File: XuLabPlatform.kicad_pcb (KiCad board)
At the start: 2 copper layers, 0 parts

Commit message: Add initial PCB layout
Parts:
- added C1: 4.7uF, Capacitor_SMD:C_0603_1608Metric, F.Cu at (143.0, 53.2)
- added C10: 100nF, Capacitor_SMD:C_0402_1005Metric, F.Cu at (122.5, 61.5)
- added C11: 22pF, Capacitor_SMD:C_0402_1005Metric, F.Cu at (141.2, 55.2)
- added C12: 22pF, Capacitor_SMD:C_0402_1005Metric, F.Cu at (137.2, 57.8)
- added C13: 100nF, Capacitor_SMD:C_0402_1005Metric, F.Cu at (167.5, 76.4)
- added C14: 100nF, Capacitor_SMD:C_0402_1005Metric, F.Cu at (165.0, 77.2)
- added C15: 1uF, Capacitor_SMD:C_0603_1608Metric, F.Cu at (129.0, 68.0)
- added C16: 10uF, Capacitor_SMD:C_1206_3216Metric, F.Cu at (130.0, 75.0)
- added C17: 100nF, Capacitor_SMD:C_0402_1005Metric, F.Cu at (129.0, 53.0)
- added C18: 100uF, Capacitor_SMD:C_1210_3225Metric, F.Cu at (161.5, 125.0)
- added C19: 10uF, Capacitor_SMD:C_1206_3216Metric, F.Cu at (165.0, 125.0)
- added C2: 100nF, Capacitor_SMD:C_0402_1005Metric, F.Cu at (144.0, 56.5)
- added C20: 1uF, Capacitor_SMD:C_0603_1608Metric, F.Cu at (163.0, 128.5)
- added C21: 10uF, Capacitor_SMD:C_1206_3216Metric, F.Cu at (150.0, 85.0)
- added C22: 100nF, Capacitor_SMD:C_0402_1005Metric, F.Cu at (152.5, 79.5)
- added C23: 22uF, Capacitor_SMD:C_0603_1608Metric, F.Cu at (154.5, 85.0)
- added C24: 22uF, Capacitor_SMD:C_0603_1608Metric, F.Cu at (154.5, 87.0)
- added C25: 100nF, Capacitor_SMD:C_0402_1005Metric, F.Cu at (158.0, 62.0)
- added C3: 100nF, Capacitor_SMD:C_0402_1005Metric, F.Cu at (146.2, 54.0)
- added C4: 100nF, Capacitor_SMD:C_0402_1005Metric, F.Cu at (156.5, 57.0)
- added C5: 100nF, Capacitor_SMD:C_0402_1005Metric, F.Cu at (155.0, 68.5)
- added C6: 100nF, Capacitor_SMD:C_0402_1005Metric, F.Cu at (147.0, 69.5)
- added C7: 2.2uF, Capacitor_SMD:C_0603_1608Metric, F.Cu at (152.8, 70.5)
- added C8: 1uF, Capacitor_SMD:C_0603_1608Metric, F.Cu at (138.5, 63.2)
- added C9: 100nF, Capacitor_SMD:C_0402_1005Metric, F.Cu at (142.5, 63.8)
- added CR1: SMBJ7.5A-13-F, XuLab:SMB_DIO, F.Cu at (150.0, 117.0)
- added CR2: MSP3V3-M3/89A, XuLab:DO-219AD_VIS, F.Cu at (161.0, 84.0)
- added D1: LED, LED_SMD:LED_0603_1608Metric, F.Cu at (158.5, 68.5)
- added D2: 75 A, Package_TO_SOT_THT:TO-247-2_Vertical, F.Cu at (155.4, 125.2)
- added D3: RCLAMP0582B, Package_TO_SOT_SMD:SOT-416, F.Cu at (163.0, 54.5)
- added FB1: 200 @ 100 MHz, Inductor_SMD:L_0805_2012Metric, F.Cu at (140.5, 63.0)
- added FL1: 0805USB-502MLC, Inductor_SMD:L_CommonModeChoke_Coilcraft_0805USB, F.Cu at (167.5, 58.5)
- added J1: SWD Connector, Connector_IDC:IDC-Header_2x05_P2.54mm_Vertical, F.Cu at (183.4, 53.6)
- added J10: Servo7, TerminalBlock_Phoenix:TerminalBlock_Phoenix_MKDS-1,5-3-5.08_1x03_P5.08mm_Horizontal, F.Cu at (185.0, 115.0)
- added J11: Servo8, TerminalBlock_Phoenix:TerminalBlock_Phoenix_MKDS-1,5-3-5.08_1x03_P5.08mm_Horizontal, F.Cu at (185.0, 98.6)
- added J12: Thruster SGN, Connector_JST:JST_VH_B3P-VH_1x03_P3.96mm_Vertical, F.Cu at (185.5, 72.5)
- added J13: USB_B_Micro, Connector_USB:USB_Micro-B_Molex_47346-0001, F.Cu at (167.4, 49.8)
- added J2: Conn_01x04, Connector_JST:JST_GH_BM04B-GHS-TBT_1x04-1MP_P1.25mm_Vertical, F.Cu at (133.0, 50.0)
- added J3: 1986660-2, XuLab:CONN2_1986660-2_TEC, F.Cu at (145.1, 133.8)
- added J4: Servo1, TerminalBlock_Phoenix:TerminalBlock_Phoenix_MKDS-1,5-3-5.08_1x03_P5.08mm_Horizontal, F.Cu at (115.0, 137.5)
- added J5: Servo2, TerminalBlock_Phoenix:TerminalBlock_Phoenix_MKDS-1,5-3-5.08_1x03_P5.08mm_Horizontal, F.Cu at (115.0, 121.0)
- added J6: Servo3, TerminalBlock_Phoenix:TerminalBlock_Phoenix_MKDS-1,5-3-5.08_1x03_P5.08mm_Horizontal, F.Cu at (115.0, 104.6)
- added J7: Servo4, TerminalBlock_Phoenix:TerminalBlock_Phoenix_MKDS-1,5-3-5.08_1x03_P5.08mm_Horizontal, F.Cu at (115.0, 88.2)
- added J8: Servo5, TerminalBlock_Phoenix:TerminalBlock_Phoenix_MKDS-1,5-3-5.08_1x03_P5.08mm_Horizontal, F.Cu at (185.0, 147.8)
- added J9: Servo6, TerminalBlock_Phoenix:TerminalBlock_Phoenix_MKDS-1,5-3-5.08_1x03_P5.08mm_Horizontal, F.Cu at (185.0, 131.4)
- added L1: 3.9uH, Inductor_SMD:L_Pulse_PA4334, F.Cu at (154.5, 82.0)
- added R1: 10k, Resistor_SMD:R_0402_1005Metric, F.Cu at (115.5, 75.0)
- added R2: 10k, Resistor_SMD:R_0402_1005Metric, F.Cu at (115.5, 82.0)
- added R3: 270, Resistor_SMD:R_0402_1005Metric, F.Cu at (141.2, 60.2)
- added R4: 4k7, Resistor_SMD:R_0402_1005Metric, F.Cu at (150.0, 52.0)
- added R5: 4k7, Resistor_SMD:R_0402_1005Metric, F.Cu at (148.0, 52.0)
- added R6: 22, Resistor_SMD:R_0402_1005Metric, F.Cu at (158.0, 59.0)
- added R7: 22, Resistor_SMD:R_0402_1005Metric, F.Cu at (158.0, 60.5)
- added R8: 75, Resistor_SMD:R_0402_1005Metric, F.Cu at (158.5, 71.5)
- added SW1: SW_Push, Button_Switch_SMD:SW_Push_1P1T_NO_E-Switch_TL3301NxxxxxG, F.Cu at (115.5, 61.5)
- added SW2: SW_SPDT, Button_Switch_SMD:Nidec_Copal_CAS-120A, F.Cu at (115.5, 71.5)
- added SW3: SW_SPDT, Button_Switch_SMD:Nidec_Copal_CAS-120A, F.Cu at (115.5, 78.5)
- added TP1: TestPoint, TestPoint:TestPoint_Plated_Hole_D2.0mm, F.Cu at (130.0, 120.0)
- added TP2: TestPoint, TestPoint:TestPoint_Plated_Hole_D2.0mm, F.Cu at (140.5, 82.5)
- added TP3: TestPoint, TestPoint:TestPoint_Plated_Hole_D2.0mm, F.Cu at (135.0, 120.0)
- added TP4: TestPoint, TestPoint:TestPoint_Plated_Hole_D2.0mm, F.Cu at (165.0, 67.5)
- added TP5: TestPoint, TestPoint:TestPoint_Plated_Hole_D2.0mm, F.Cu at (135.5, 82.5)
- added U1: STM32F446RCTx, Package_QFP:LQFP-64_10x10mm_P0.5mm, F.Cu at (150.0, 62.0)
- added U2: ISM330DHCX, Package_LGA:LGA-14_3x2.5mm_P0.5mm_LayoutBorder3x4y, F.Cu at (165.0, 75.0)
- added U3: MMC5983MA, XuLab:MMC5983MA_MEM, F.Cu at (130.0, 71.0)
- added U4: AP63203WU, Package_TO_SOT_SMD:TSOT-23-6, F.Cu at (150.0, 82.0)
- added U5: TVS0500DRV, Package_SON:WSON-6-1EP_2x2mm_P0.65mm_EP1x1.6mm, F.Cu at (171.0, 54.0)
- added Y1: 25 MHz, Crystal:Crystal_SMD_Abracon_ABM8G-4Pin_3.2x2.5mm, F.Cu at (140.2, 57.8)
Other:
- board outline added: 83 x 105 mm

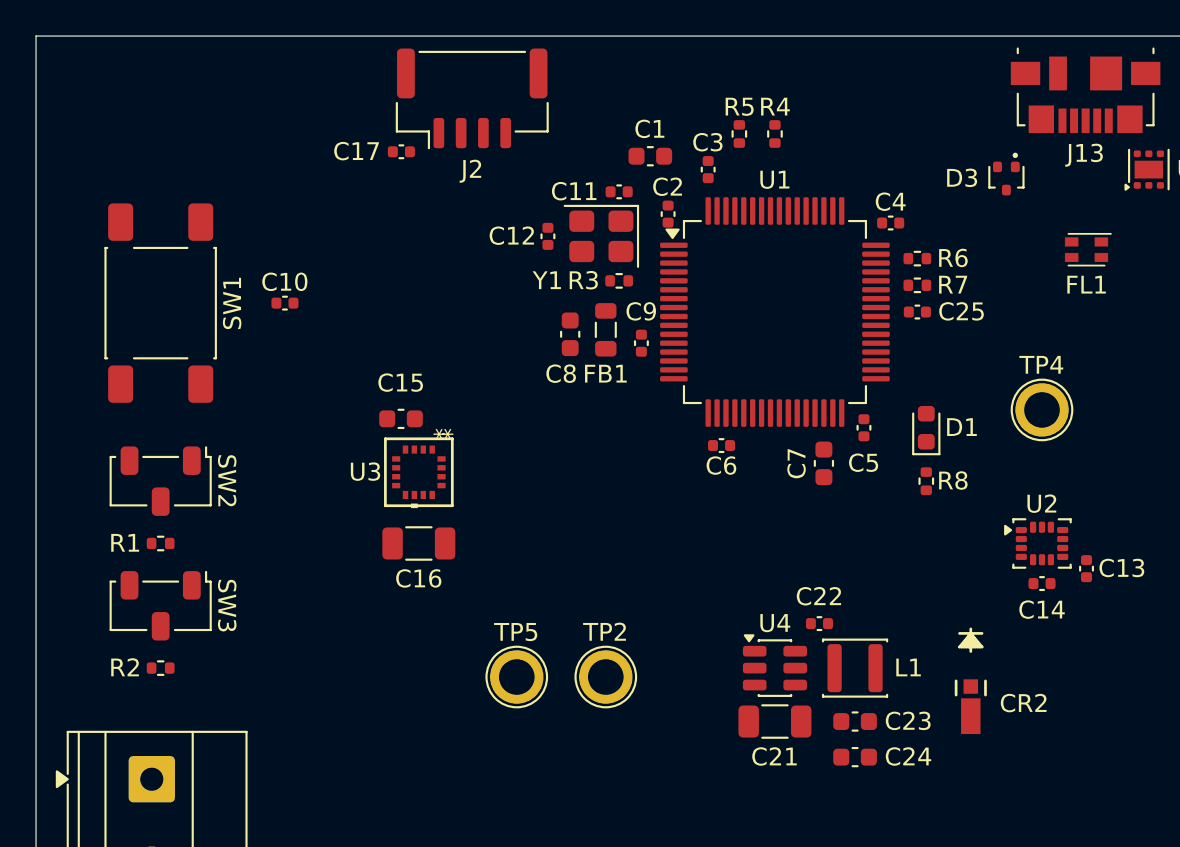
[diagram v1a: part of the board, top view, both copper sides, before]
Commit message: Change ferrite bead with TLV1117LV33 LDO for 3.3VA filtering
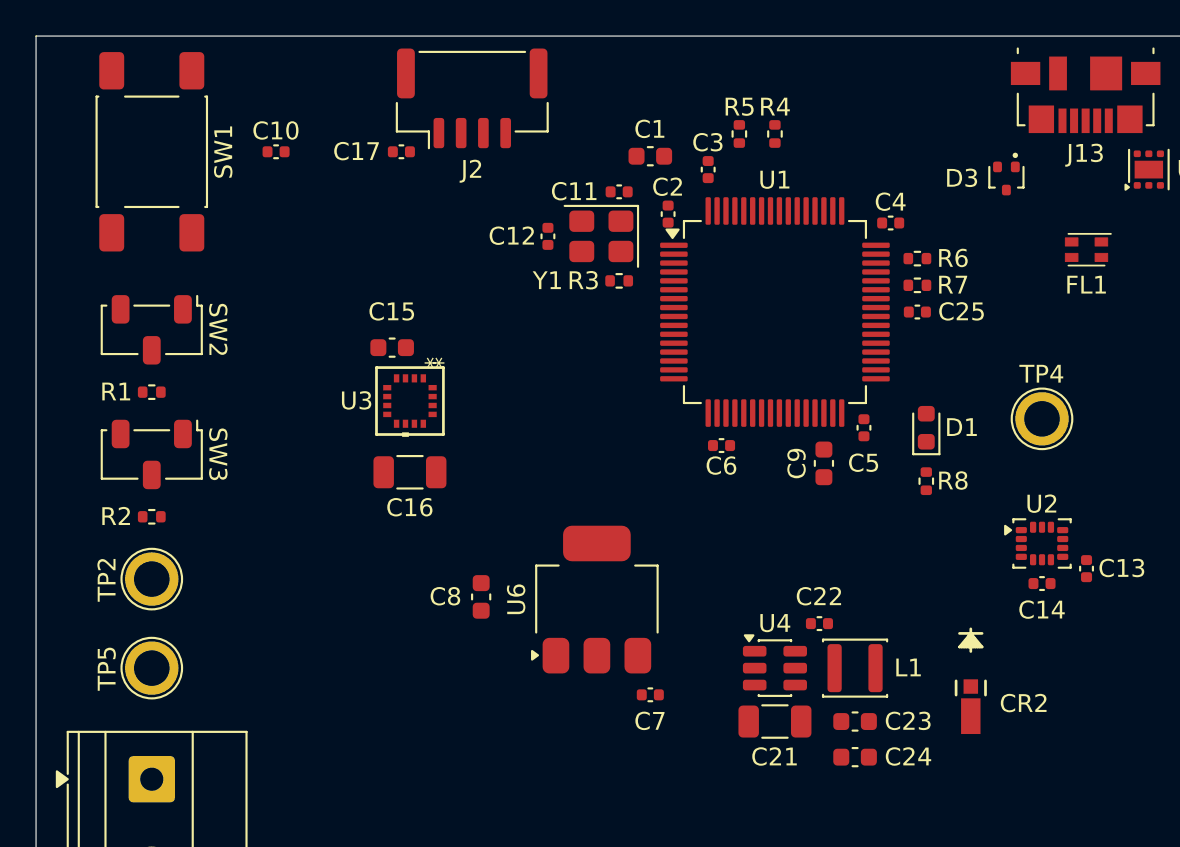
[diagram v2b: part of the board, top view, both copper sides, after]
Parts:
- removed FB1: 200 @ 100 MHz, Inductor_SMD:L_0805_2012Metric
- added U6: TLV1117LV33, Package_TO_SOT_SMD:SOT-223-3_TabPin2, F.Cu at (140.0, 78.2)
- moved TP2 26.1 mm to (115.0, 77.0), turned to 180 degrees
- moved TP5 20.5 mm to (115.0, 82.0), turned to 90 degrees
- moved C7 19.8 mm to (143.0, 83.5), turned to 0 degrees
- moved C8 15.6 mm to (133.5, 78.0), turned to -90 degrees
- moved C10 8.51 mm to (122.0, 53.0)
- moved R1 8.51 mm to (115.0, 66.5)
- moved R2 8.51 mm to (115.0, 73.5)
- moved SW1 8.51 mm to (115.0, 53.0)
- moved SW2 8.51 mm to (115.0, 63.0)
- moved SW3 8.51 mm to (115.0, 70.0)
- moved C15 4.03 mm to (128.5, 64.0)
- moved C16 4.03 mm to (129.5, 71.0)
- moved U3 4.03 mm to (129.5, 67.0)
- moved TP4 0.50 mm to (165.0, 68.0)
- renumbered C9 to C7, C7 to C9
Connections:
- C7 pad 1: +3.3VA -> +3.3V

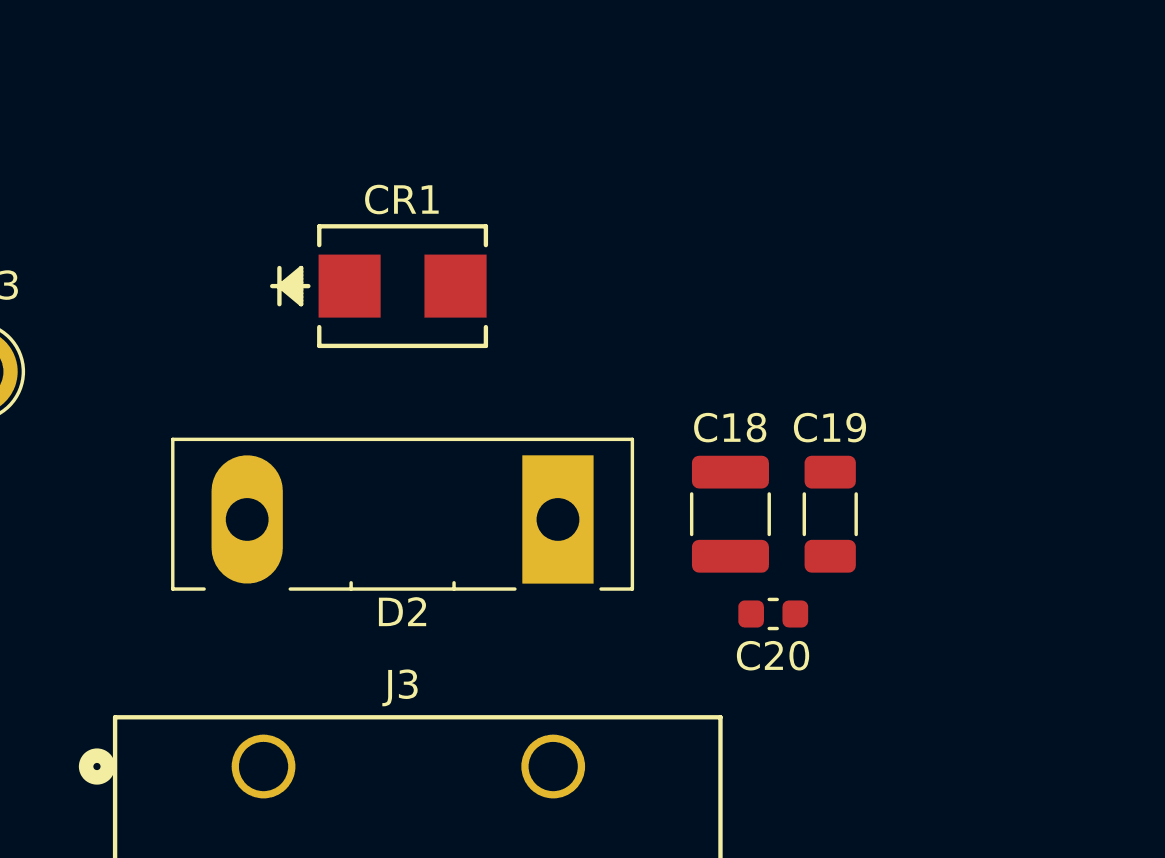
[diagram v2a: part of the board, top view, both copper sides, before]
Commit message: Replace Schottky diode with P-channel mosfet circuit
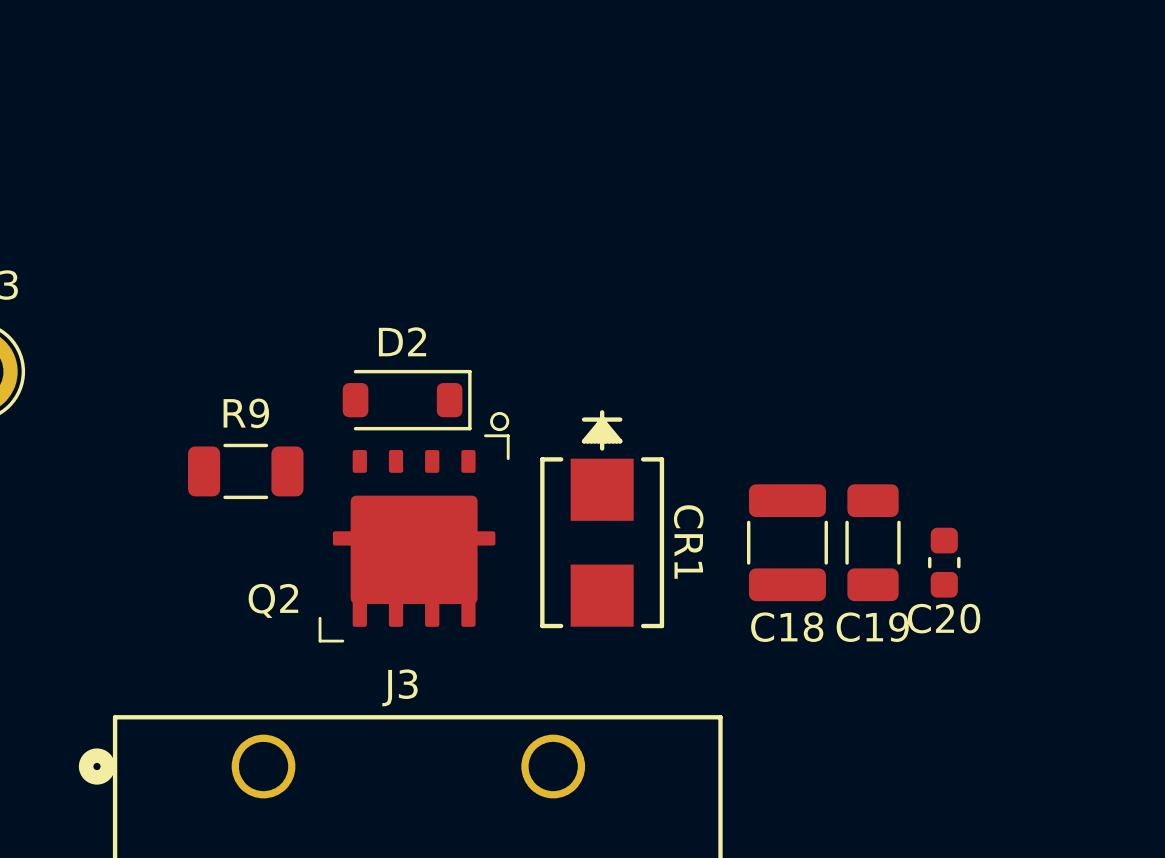
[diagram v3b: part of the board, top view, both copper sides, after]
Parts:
- added Q2: PMOS, XuLab:SOP-Advance-8, F.Cu at (150.4, 125.8)
- added R9: 75, Resistor_SMD:R_1206_3216Metric, F.Cu at (144.5, 123.5)
- CR1: value SMBJ7.5A-13-F -> 7.5V
- CR2: value MSP3V3-M3/89A -> 3.3V
- D2: value 75 A -> 4.7V; footprint Package_TO_SOT_THT:TO-247-2_Vertical -> Diode_SMD:D_SOD-123
- moved CR1 11.4 mm to (157.0, 126.0), turned to -90 degrees
- moved D2 6.87 mm to (150.0, 121.0)
- moved C20 6.26 mm to (169.0, 126.7), turned to -90 degrees
- moved C18 2.24 mm to (163.5, 126.0)
- moved C19 1.80 mm to (166.5, 126.0)
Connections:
- J3 pad 1A: Net-(D2-A) -> Net-(Q2-D)
- J3 pad 1B: Net-(D2-A) -> Net-(Q2-D)

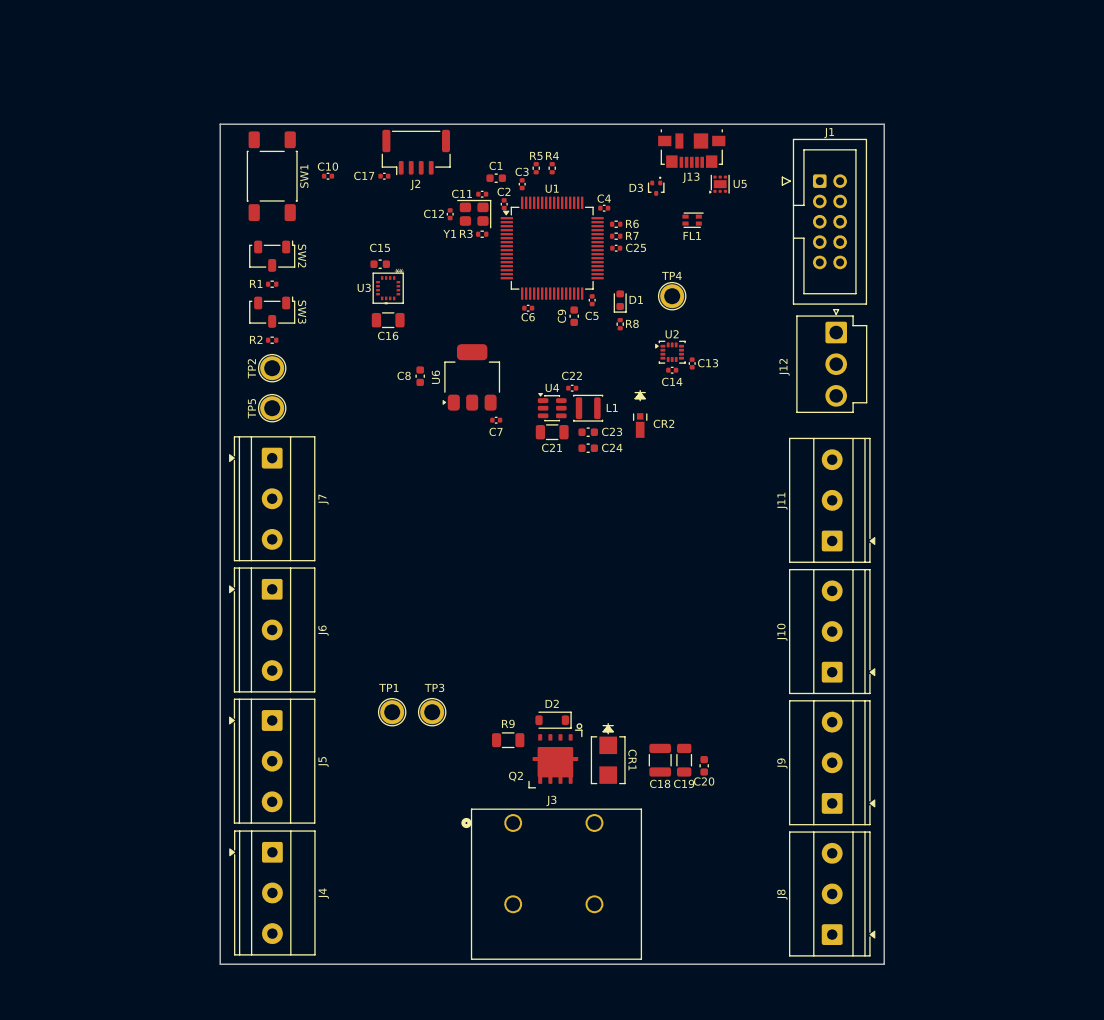
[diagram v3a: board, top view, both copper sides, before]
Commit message: Add breakout sockets for microcontroller IO lines
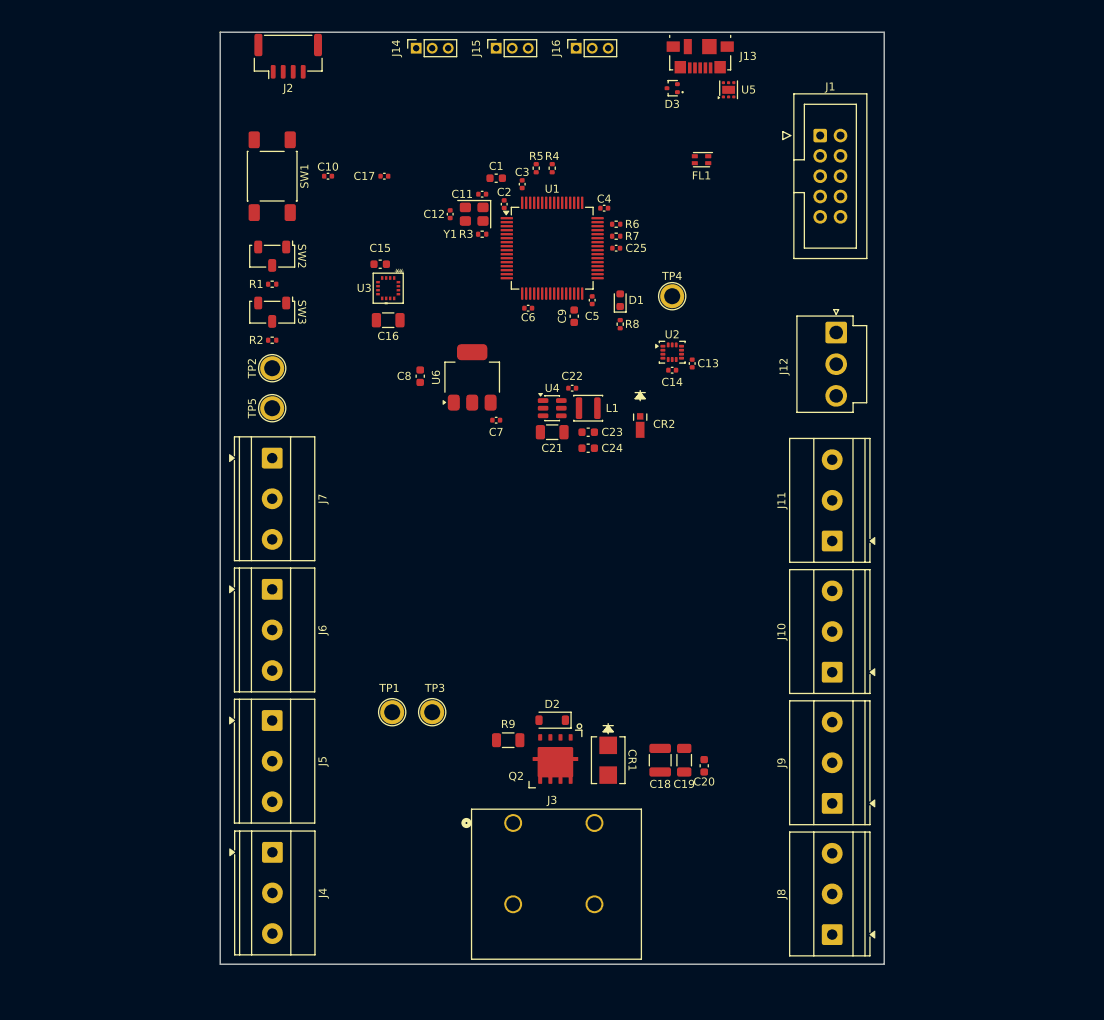
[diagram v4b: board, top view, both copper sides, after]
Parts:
- added J14: CAN, Connector_PinSocket_2.00mm:PinSocket_1x03_P2.00mm_Vertical, F.Cu at (133.0, 37.0)
- added J15: I2C, Connector_PinSocket_2.00mm:PinSocket_1x03_P2.00mm_Vertical, F.Cu at (143.0, 37.0)
- added J16: UART, Connector_PinSocket_2.00mm:PinSocket_1x03_P2.00mm_Vertical, F.Cu at (153.0, 37.0)
- moved J2 20.0 mm to (117.0, 38.0)
- moved D3 12.7 mm to (165.0, 42.0), turned to 180 degrees
- moved J13 11.8 mm to (168.5, 38.0)
- moved U5 11.8 mm to (172.1, 42.2)
- moved FL1 7.65 mm to (168.7, 50.9)
- moved J1 5.70 mm to (183.5, 47.9)
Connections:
- U1 pad 51: /MCU A/UART4_TX -> /UART_TX
- U1 pad 52: /MCU A/UART4_RX -> /UART_RX
- U1 pad 61: /MCU A/CAN1_RX -> /CAN1_RX
- U1 pad 62: /MCU A/CAN1_TX -> /CAN1_TX
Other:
- board size 83 x 105 mm -> 83 x 116.5 mm

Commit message: Update layout
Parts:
- moved R1 95.6 mm to (210.0, 55.6)
- moved R2 95.6 mm to (210.0, 62.6)
- moved SW2 95.6 mm to (210.0, 52.1)
- moved SW3 95.6 mm to (210.0, 59.1)
- moved J12 72.5 mm to (189.0, 145.0), turned to 180 degrees
- moved TP5 64.3 mm to (175.0, 105.0), turned to 180 degrees
- moved TP2 59.5 mm to (167.5, 105.0), turned to -90 degrees
- moved C15 46.8 mm to (175.2, 62.0)
- moved C16 45.8 mm to (175.2, 69.2)
- moved U3 45.8 mm to (175.2, 65.2)
- moved C10 33.9 mm to (90.0, 64.2)
- moved C17 30.8 mm to (99.0, 46.2), turned to 0 degrees
- moved J11 29.9 mm to (210.5, 82.9)
- moved J1 29.6 mm to (154.9, 40.2), turned to 90 degrees
- moved J7 29.4 mm to (89.5, 73.7)
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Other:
- board size 83 x 116.5 mm -> 134 x 123.5 mm
